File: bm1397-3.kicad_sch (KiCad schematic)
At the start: 101 parts, among them IC1 BM1397_mode1, J3 Conn_01x05, U3 SN74LVC1T45DBVR, U5 MCP1824T-1802E, U5 SN74LVC1T45DBVR, U6 MCP1824T-0802E, U8 SN74LVC1T45DBVR, X1 OT322525MJBA4SL

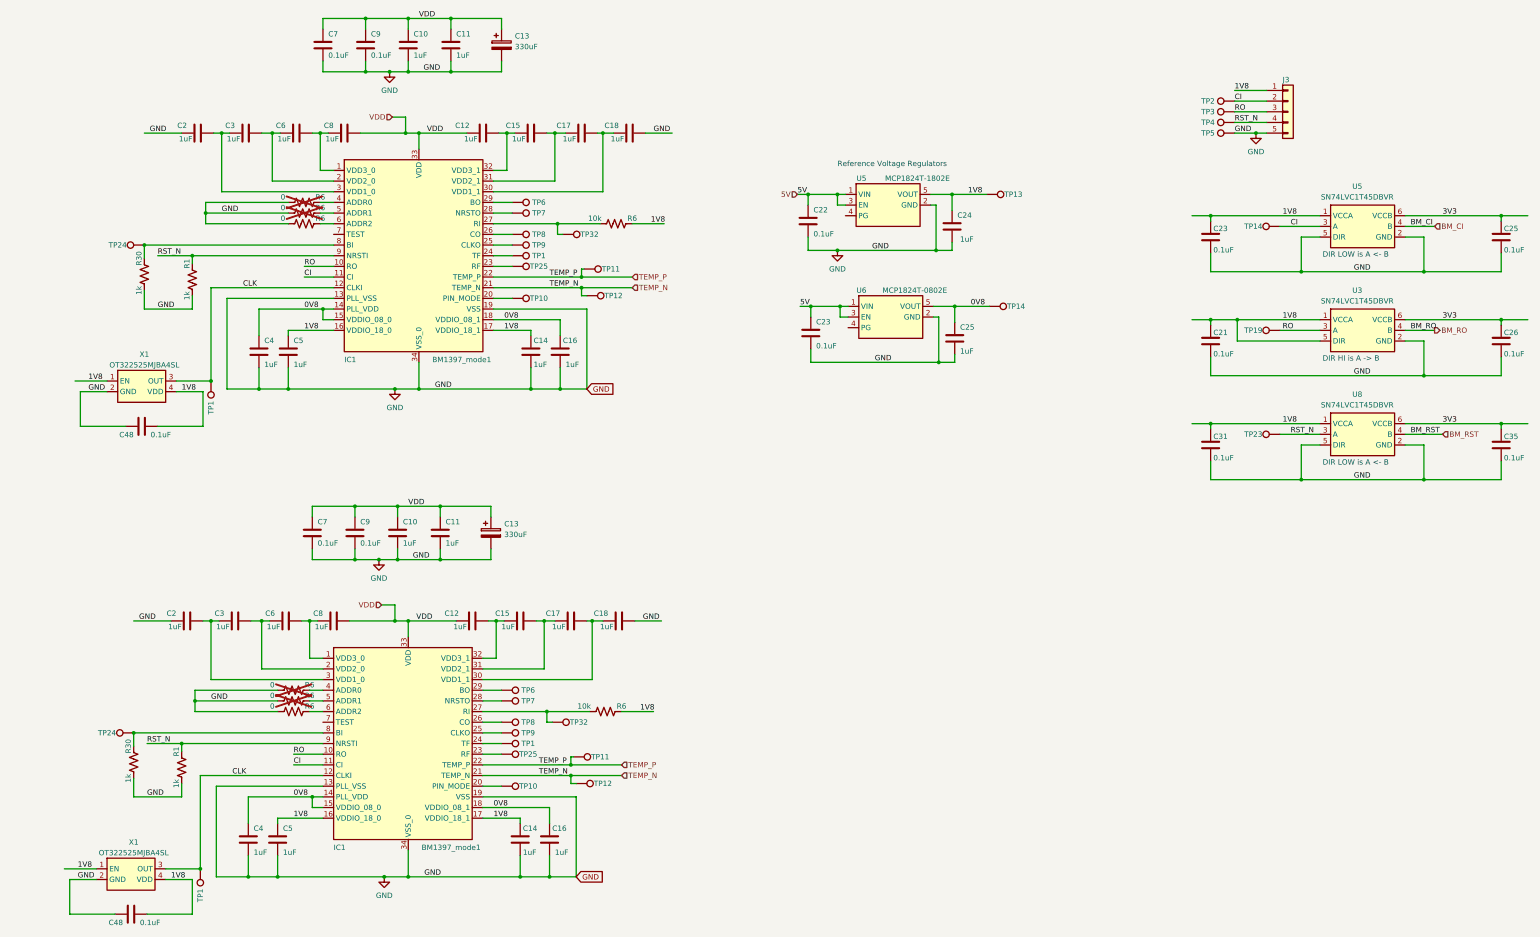
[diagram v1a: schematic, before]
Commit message: starting to sort out the asic data connections
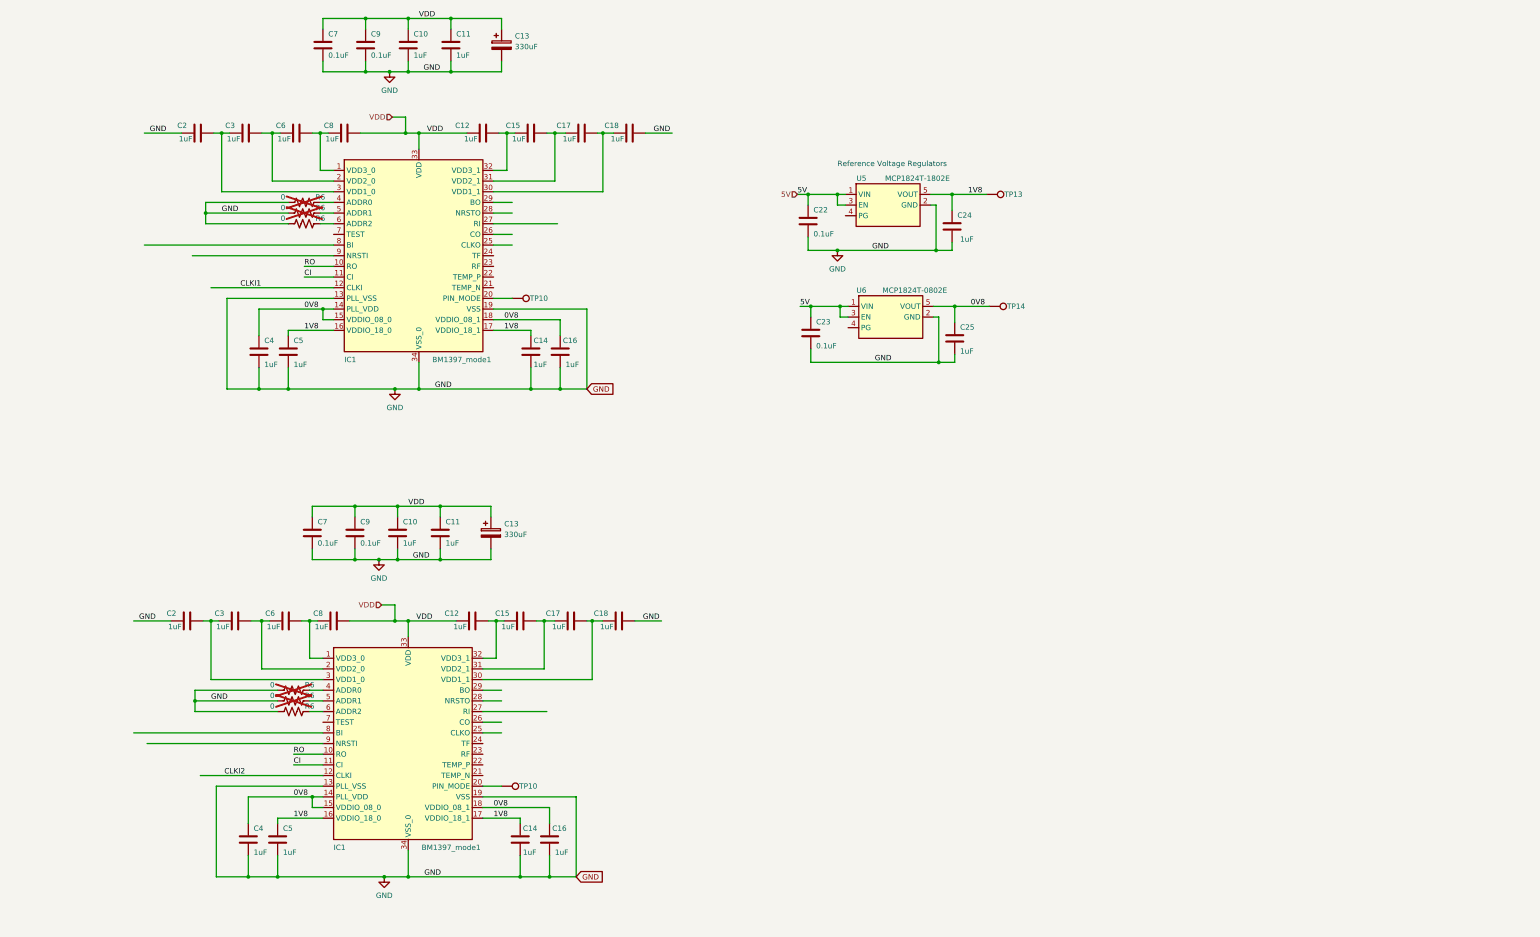
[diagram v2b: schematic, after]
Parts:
- removed C21, C23, C25, C26, C31, C35, C48 (x2): 311-3342-1-ND, Capacitor_SMD:C_0402_1005Metric, symbol Device:C
- removed J3: Conn_01x05, Connector_PinHeader_2.54mm:PinHeader_1x05_P2.54mm_Vertical, symbol Connector_Generic:Conn_01x05
- removed R1 (x2), R30 (x2): 1k, Resistor_SMD:R_0402_1005Metric, symbol Device:R_US
- removed R6 (x2): 10k, Resistor_SMD:R_0402_1005Metric, symbol Device:R_US
- removed TP1 (x4), TP11 (x2), TP12 (x2), TP14, TP19, TP2, TP23, TP24 (x2), TP25 (x2), TP3, TP32 (x2), TP4, TP5, TP6 (x2), TP7 (x2), TP8 (x2), TP9 (x2): TestPoint, TestPoint:TestPoint_Pad_D1.5mm, symbol Connector:TestPoint
- removed U3, U5, U8: SN74LVC1T45DBVR, lcsc:SOT-23-6_L2.9-W1.6-P0.95-LS2.8-BR, symbol lcsc:SN74LVC1T45DBVR
- removed X1 (x2): OT322525MJBA4SL, lcsc:OSC-SMD_4P-L3.2-W2.5-BL, symbol lcsc:OT322525MJBA4SL
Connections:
- net CLK renamed CLKI1
- net CLKI1: no longer IC1.12 (CLKI)
- net RST_N: no longer names the net of IC1.9 (NRSTI)
- net RST_N: no longer IC1.9 (NRSTI)
- net TEMP_N: no longer names the net of IC1.21 (TEMP_N)
- net TEMP_N: no longer IC1.21 (TEMP_N)
- net TEMP_P: no longer names the net of IC1.22 (TEMP_P)
- net TEMP_P: no longer IC1.22 (TEMP_P)
- new net CLKI2: IC1.12 (CLKI)
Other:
- note removed: "DIR HI is A -> B"
- note removed: "DIR LOW is A <- B"

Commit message: connected up power and data to ASICs in schematic
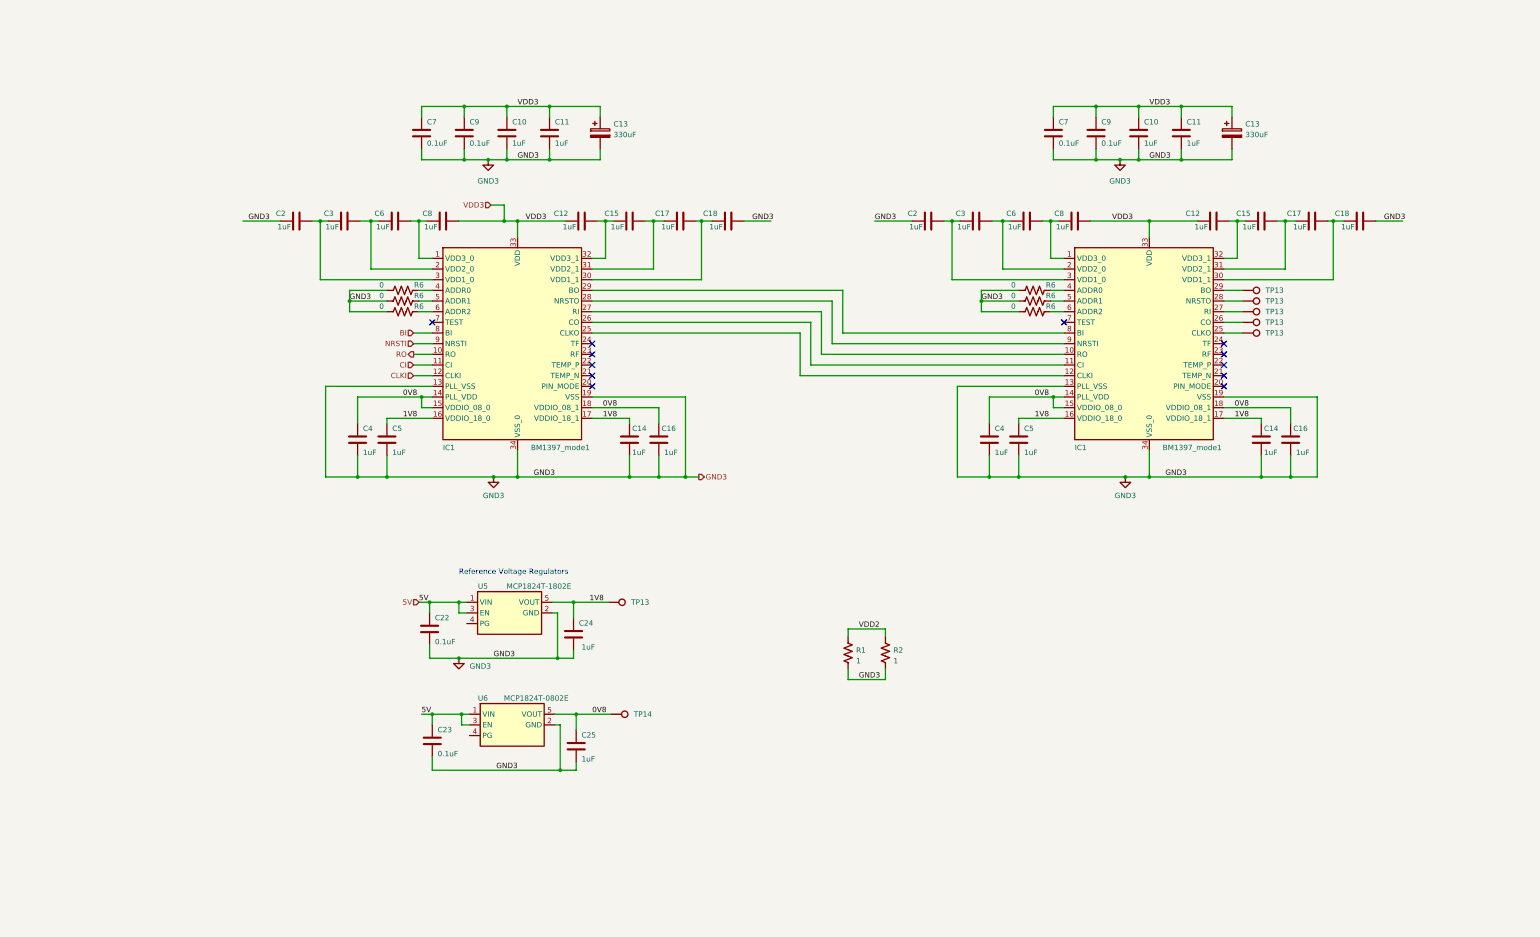
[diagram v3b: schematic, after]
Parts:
- removed C10 (x2), C11 (x2), C12 (x2), C14 (x2), C15 (x2), C16 (x2), C17 (x2), C18 (x2), C2 (x2), C3 (x2), C4 (x2), C5 (x2), C6 (x2), C8 (x2): 587-5514-1-ND, Capacitor_SMD:C_0402_1005Metric, symbol Device:C
- removed C13 (x2): 330uF, Capacitor_Tantalum_SMD:CP_EIA-7343-31_Kemet-D_Pad2.25x2.55mm_HandSolder, symbol Device:C_Polarized
- removed C7 (x2), C9 (x2): 311-3342-1-ND, Capacitor_SMD:C_0402_1005Metric, symbol Device:C
- removed IC1 (x2): BM1397_mode1, bitaxe:BM1397, symbol bitaxe:BM1397_mode1
- removed R6 (x6): 0, Resistor_SMD:R_0402_1005Metric, symbol Device:R_US
- removed TP10 (x2): TestPoint, TestPoint:TestPoint_Pad_D1.5mm, symbol Connector:TestPoint
- added C10 (x2), C11 (x2), C12 (x2), C14 (x2), C15 (x2), C16 (x2), C17 (x2), C18 (x2), C2 (x2), C3 (x2), C4 (x2), C5 (x2), C6 (x2), C8 (x2): 587-5514-1-ND, Capacitor_SMD:C_0402_1005Metric, symbol Device:C
- added C13 (x2): 330uF, Capacitor_Tantalum_SMD:CP_EIA-7343-31_Kemet-D_Pad2.25x2.55mm_HandSolder, symbol Device:C_Polarized
- added C7 (x2), C9 (x2): 311-3342-1-ND, Capacitor_SMD:C_0402_1005Metric, symbol Device:C
- added IC1 (x2): BM1397_mode1, bitaxe:BM1397, symbol bitaxe:BM1397_mode1
- added R1, R2: 1, Resistor_SMD:R_2512_6332Metric, symbol Device:R_US
- added R6 (x6): 0, Resistor_SMD:R_0402_1005Metric, symbol Device:R_US
- added TP13 (x5): TestPoint, TestPoint:TestPoint_Pad_D1.5mm, symbol Connector:TestPoint
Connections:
- net 0V8: now also C16.1, C16.1, C4.1, C4.1, IC1.14 (PLL_VDD), IC1.14 (PLL_VDD), IC1.15 (VDDIO_08_0), IC1.15 (VDDIO_08_0), IC1.18 (VDDIO_08_1), IC1.18 (VDDIO_08_1)
- net 1V8: now also C14.1, C14.1, C5.1, C5.1, IC1.16 (VDDIO_18_0), IC1.16 (VDDIO_18_0), IC1.17 (VDDIO_18_1), IC1.17 (VDDIO_18_1)
- net CI: now also IC1.11 (CI)
- net GND: now also C10.2, C10.2, C11.2, C11.2, C13.2, C13.2, C14.2, C14.2, C16.2, C16.2, C18.2, C18.2, C2.1, C2.1, C4.2, C4.2, C5.2, C5.2, C7.2, C7.2, C9.2, C9.2, IC1.13 (PLL_VSS), IC1.13 (PLL_VSS), IC1.19 (VSS), IC1.19 (VSS), IC1.34 (VSS_0), IC1.34 (VSS_0), R1.2, R2.2, R6.1, R6.1, R6.1, R6.1, R6.1, R6.1
- net RO: now also IC1.10 (RO)
- new net: C6.2, C8.1, IC1.1 (VDD3_0) (x2)
- new net: IC1.26 (CO), TP13.1
- new net: IC1.5 (ADDR1), R6.2 (x2)
- new net: C2.2, C3.1, IC1.3 (VDD1_0) (x2)
- new net: IC1.27 (RI), TP13.1
- new net: IC1.29 (BO), TP13.1
- new net: IC1.6 (ADDR2), R6.2 (x2)
- new net: C17.2, C18.1, IC1.30 (VDD1_1) (x2)
- new net: IC1.4 (ADDR0), R6.2 (x2)
- new net: IC1.25 (CLKO), TP13.1
- new net: C3.2, C6.1, IC1.2 (VDD2_0) (x2)
- new net: IC1.12 (CLKI), IC1.25 (CLKO)
- new net: IC1.11 (CI), IC1.26 (CO)
- new net: IC1.10 (RO), IC1.27 (RI)
- new net: IC1.28 (NRSTO), IC1.9 (NRSTI)
- new net: IC1.29 (BO), IC1.8 (BI)
- new net: C15.2, C17.1, IC1.31 (VDD2_1) (x2)
- new net: C12.2, C15.1, IC1.32 (VDD3_1) (x2)
- new net: IC1.28 (NRSTO), TP13.1
- new net BI: IC1.8 (BI)
- new net CLKI: IC1.12 (CLKI)
- new net NRSTI: IC1.9 (NRSTI)
- new net VDD2: R1.1, R2.1
- new net VDD3: C10.1, C10.1, C11.1, C11.1, C12.1, C12.1, C13.1, C13.1, C7.1, C7.1, C8.2, C8.2, C9.1, C9.1, IC1.33 (VDD), IC1.33 (VDD)
- no-connect marks 0 -> 12
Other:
- moved on the sheet: C22, C23, C24, C25, TP13, TP14, U5, U6

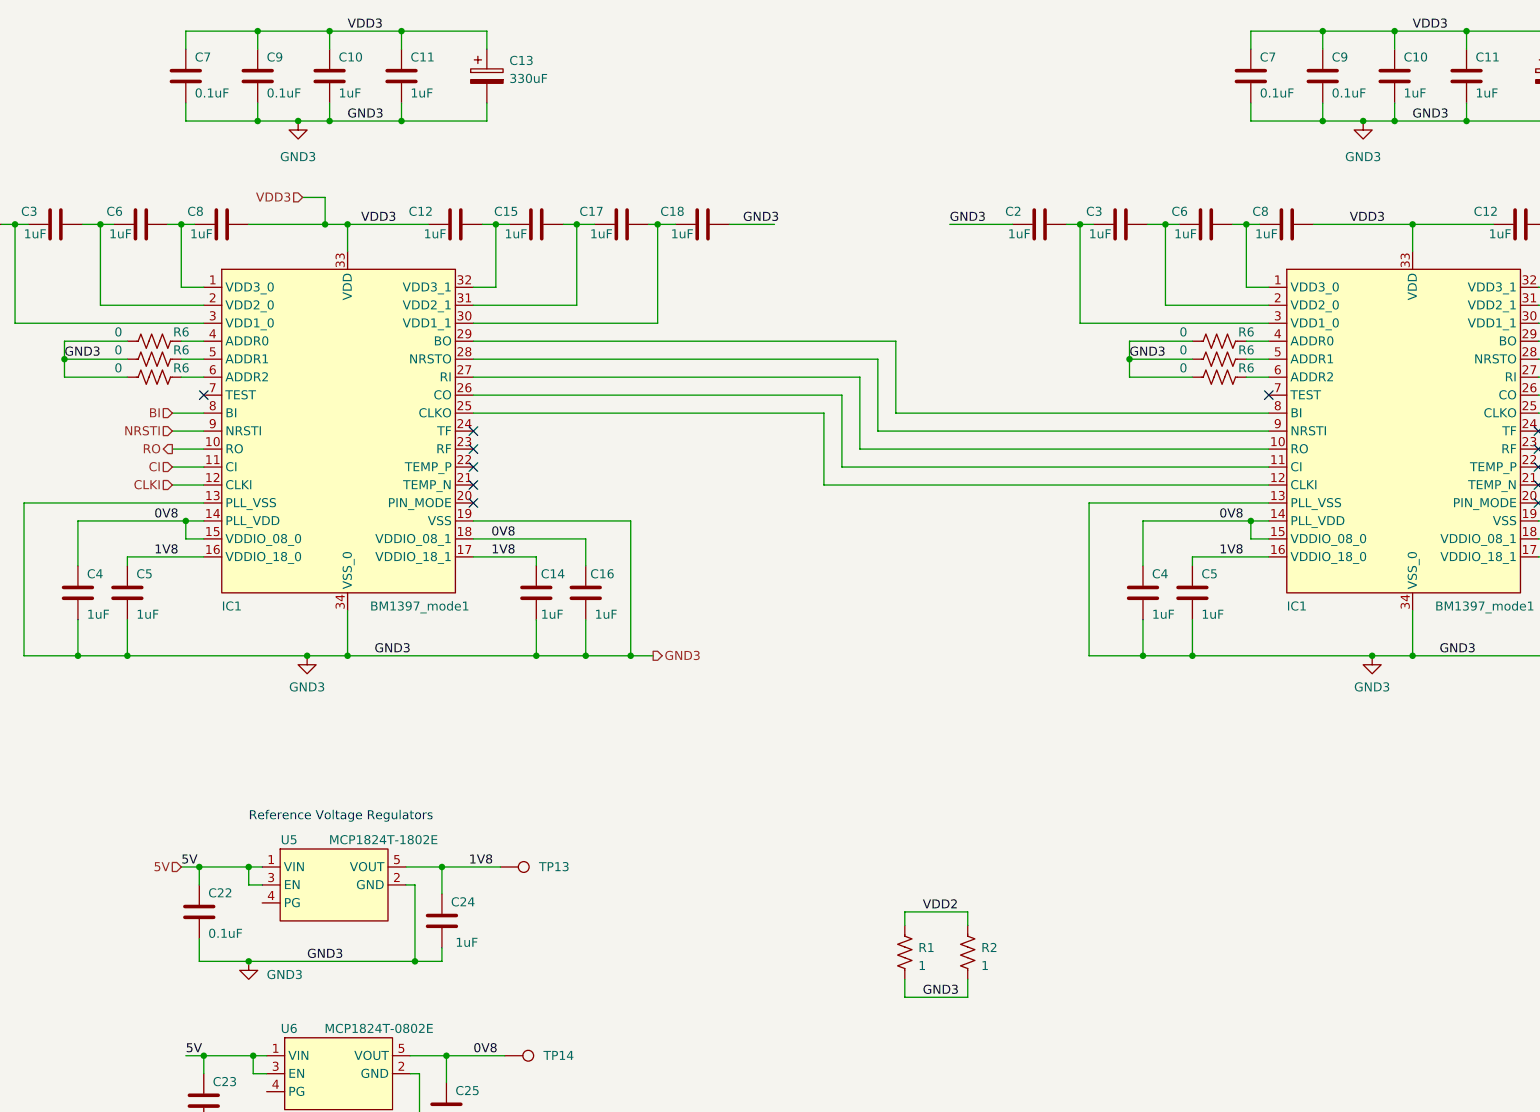
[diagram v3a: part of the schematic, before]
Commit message: fixed the floating gnd net issue. started placement
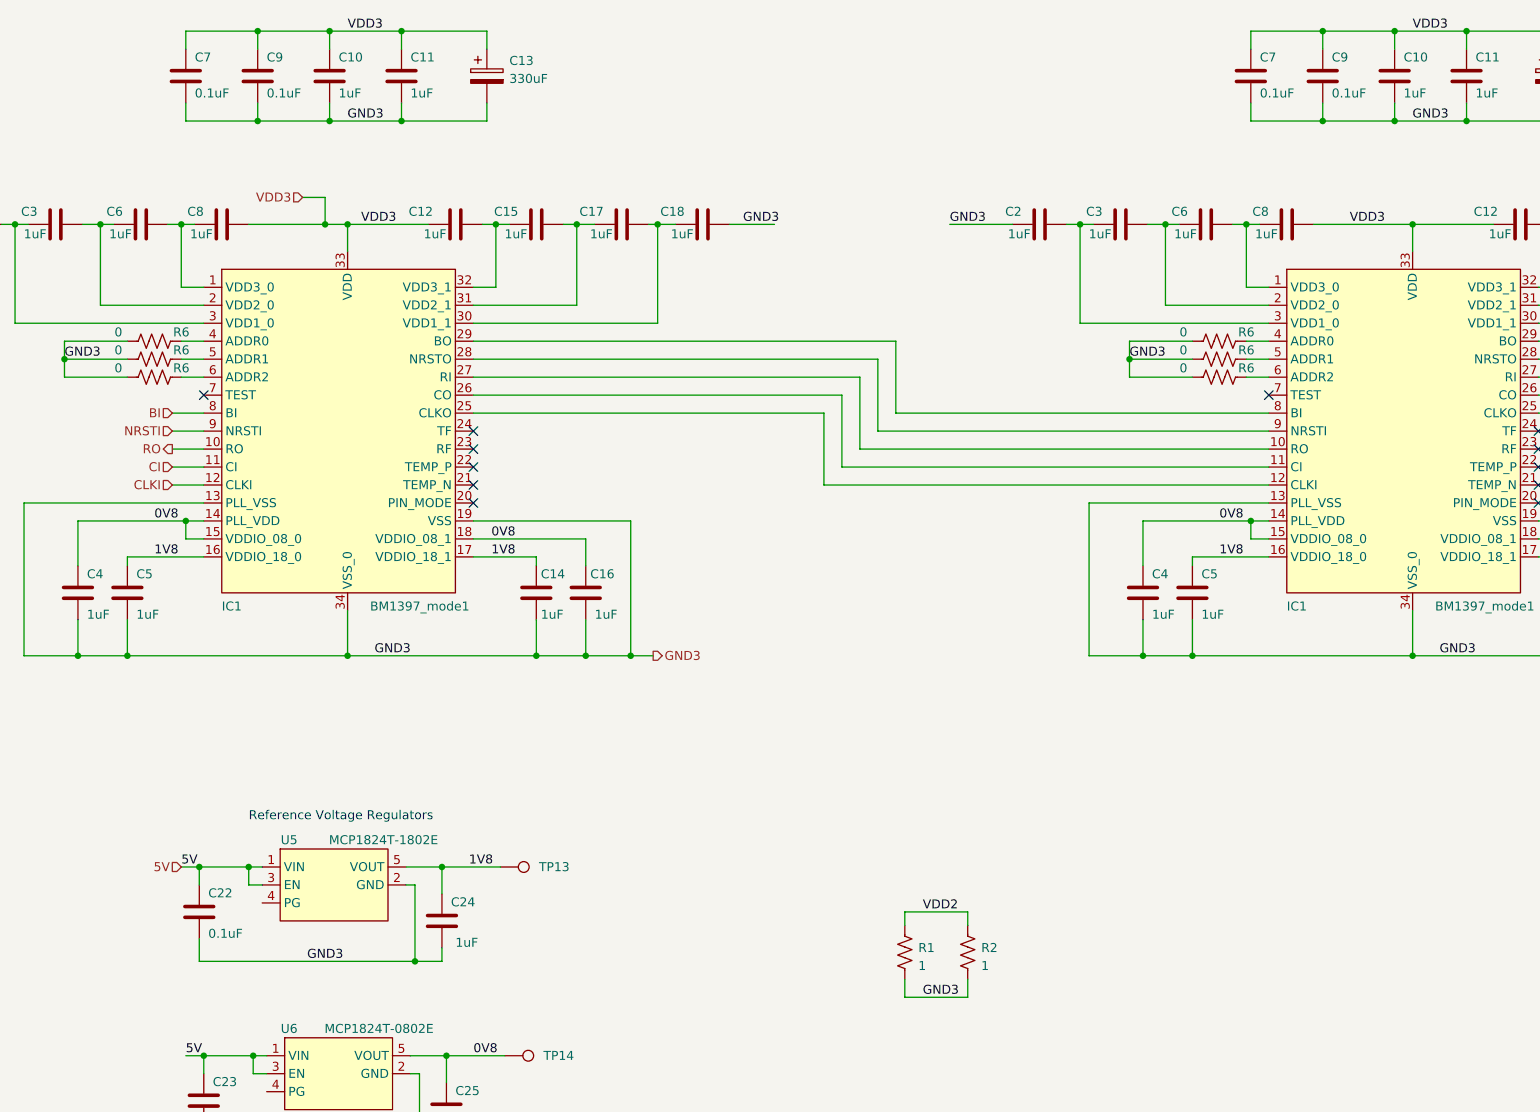
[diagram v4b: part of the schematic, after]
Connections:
- net GND renamed GND3
